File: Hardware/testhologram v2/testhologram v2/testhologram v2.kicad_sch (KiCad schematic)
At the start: 609 parts, among them U1 SM16106SC, U10 SM16106SC, U11 SM16106SC, U12 SM16106SC, U13 SM16106SC, U14 SM16106SC, U15 SM16106SC, U16 SM16106SC, U17 SM16106SC, U18 SM16106SC, U19 SM16106SC, U2 SM16106SC, U20 SM16106SC, U21 SM16106SC, U22 SM16106SC, U23 SM16106SC, U24 SM16106SC, U25 SM16106SC, U26 SM16106SC, U27 SM16106SC, U28 SM16106SC, U29 SM16106SC, U3 SM16106SC, U30 SM16106SC, U31 SM16106SC, U32 SM16106SC, U33 ESP32-S3-WROOM-1(N16R8), U4 SM16106SC, U5 SM16106SC, U6 SM16106SC, U7 SM16106SC, U8 SM16106SC, U9 SM16106SC

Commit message: added esp32 devboard docs into dataheets folder, updated hologram kicad schematic
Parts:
- added C33: 22uF/25v, symbol Device:C_Small
- added C34, C37, C38: 0.1uF/50v, symbol Device:C_Small
- added C35: 1uF/16v, symbol Device:C_Small
- added C36: 10uF/25v, symbol Device:C_Small
- added D1: 1N5819HW-7-F, symbol Device:D
- added D2, D3, D4: LESD5Z5.0CT1G, symbol Device:D_TVS
- added J1: USB_C_Receptacle_USB2.0_16P, symbol Connector:USB_C_Receptacle_USB2.0_16P
- added R33: 1M, symbol Device:R_Small_US
- added R34: 10k, symbol Device:R_Small_US
- added R35, R36: 5.11k, symbol Device:R_Small_US
- added SW1: SW_Reset, symbol Switch:SW_Push
- added SW2: SW_Boot, symbol Switch:SW_Push
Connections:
- net GND: now also U33.1 (GND), U33.40 (GND), U33.41 (GND), C33.2, C34.2, C35.2, C36.2, C37.2, C38.2, D2.1 (A1), D3.1 (A1), D4.1 (A1), J1.A1 (GND), J1.A12 (GND), J1.B1 (GND), J1.B12 (GND), R33.2, R35.2, R36.2, SW1.1, SW2.1
- net USB_D-: now reaches U33.13 (IO19)
- net USB_D-: now also D3.2 (A2), J1.A7 (D-), J1.B7 (D-)
- net USB_D+: now reaches U33.14 (IO20)
- net USB_D+: now also D4.2 (A2), J1.A6 (D+), J1.B6 (D+)
- net +3.3V: now reaches U33.2 (3V3)
- net +3.3V: now also C33.1, C34.1, R34.1
- net at U33.27 (IO0): now also C37.1, SW2.2
- net at U33.3 (EN): now also C35.1, C38.1, R34.2, SW1.2
- new net: J1.A5 (CC1), R35.1
- new net: D1.2 (A), D2.2 (A2), J1.A4 (VBUS), J1.A9 (VBUS), J1.B4 (VBUS), J1.B9 (VBUS)
- new net: J1.B5 (CC2), R36.1
- new net: J1.S1 (SHIELD), R33.1
- new net +5V: C36.1, D1.1 (K)
- no-connect marks 1 -> 8
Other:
- company: (none) -> Kaden Sparrow
- title: (none) -> Hologram spinnig panel

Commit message: worked on kicad
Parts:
- removed C37: 0.1uF/50v, symbol Device:C_Small
- added C39: 0.1uF/50v, symbol Device:C_Small
- added D5, D6, D7, D8: LESD5Z5.0CT1G, symbol Device:D_TVS
- added J2: Conn_01x06_Socket, symbol Connector:Conn_01x06_Socket
- added R37, R38, R39: 2.2k, symbol Device:R_Small_US
- added R40: 100k, symbol Device:R_Small_US
- added R41, R42, R43, R44, R45, R46: 33, symbol Device:R_Small_US
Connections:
- net +3.3V: now also R37.2, R38.2, R39.2
- net GND: now also C39.2, D5.1 (A1), D6.1 (A1), D7.1 (A1), D8.1 (A1), J2.2 (Pin_2), R40.1
- net USB_D+: now also R46.2; no longer U33.14 (IO20)
- net USB_D-: now also R45.2; no longer U33.13 (IO19)
- net VCC: now also J2.3 (Pin_3)
- net at U33.27 (IO0): now also R41.2; no longer SW2.2
- net SW_Reset: now reaches C35.1, C38.1, R34.2, SW1.2, U33.3 (EN)
- net at U33.4 (IO4): now also R42.1
- net at U33.5 (IO5): now also R43.1
- net at U33.6 (IO6): now also R44.1
- new net: R45.1, U33.13 (IO19)
- new net: R46.1, U33.14 (IO20)
- new net: D8.2 (A2), J2.1 (Pin_1), R40.2
- new net ENC_A: D5.2 (A2), J2.6 (Pin_6), R39.1, R42.2
- new net ENC_B: D6.2 (A2), J2.5 (Pin_5), R38.1, R43.2
- new net ENC_Z: D7.2 (A2), J2.4 (Pin_4), R37.1, R44.2
- new net SW_Boot: C39.1, R41.1, SW2.2
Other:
- note added: "1 PWM 2 GND 3 V+ 4 Z 5 B 6 A"
- moved on the sheet: C34, C35, C38, SW1

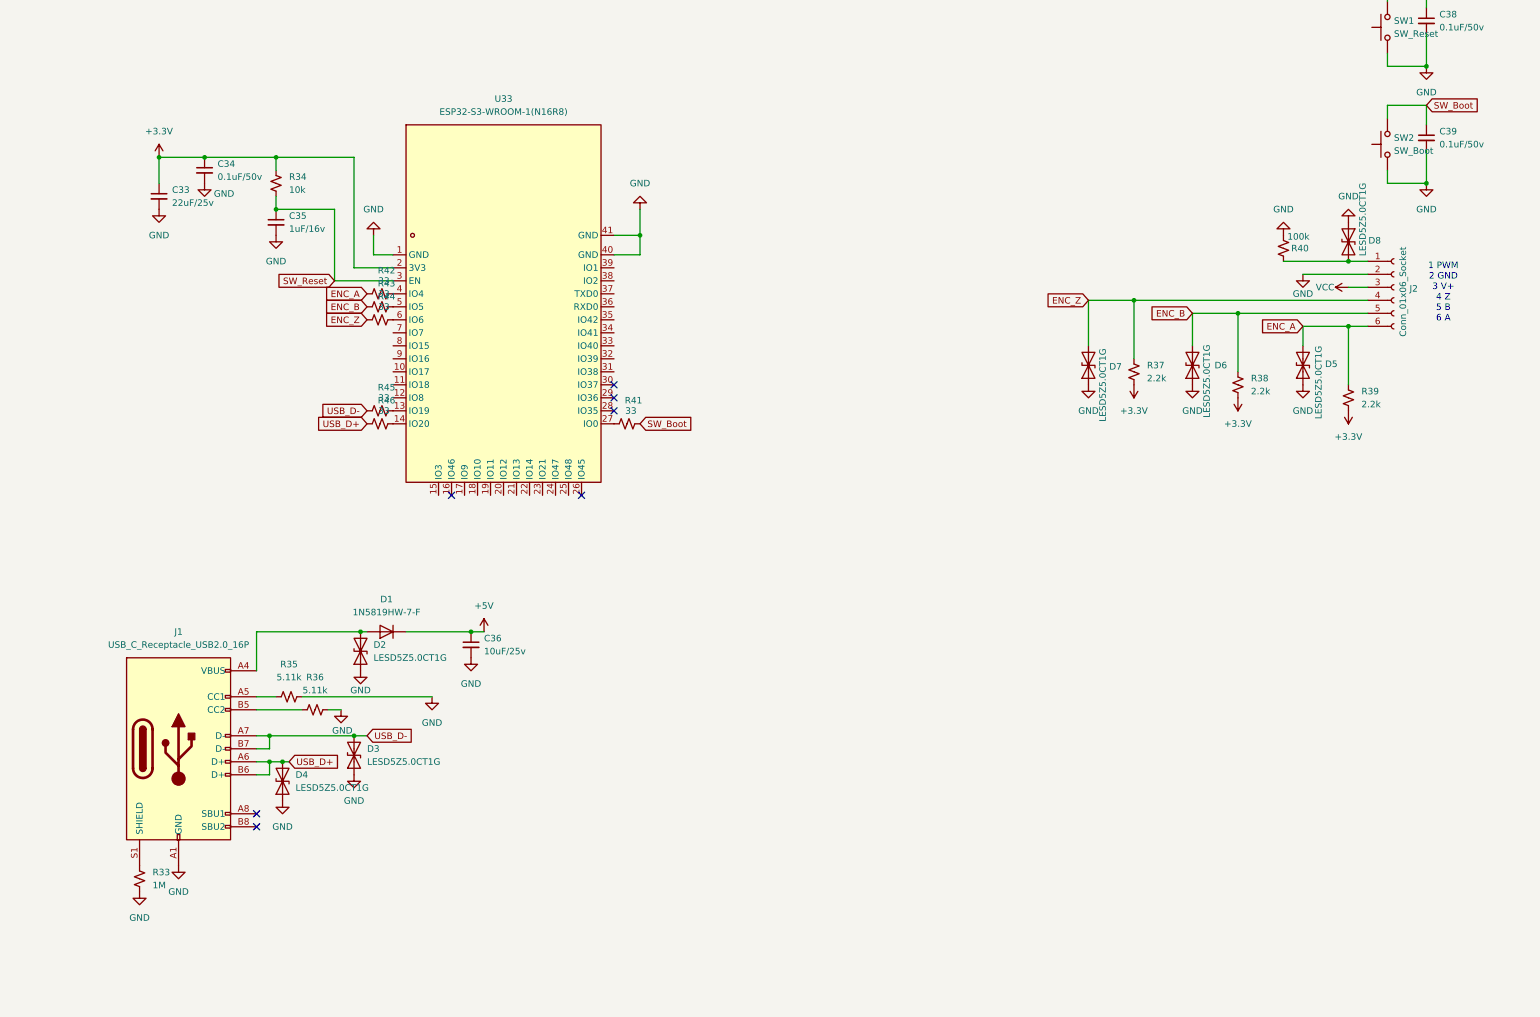
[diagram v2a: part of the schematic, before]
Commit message: added parts to schematic. added footprints/models
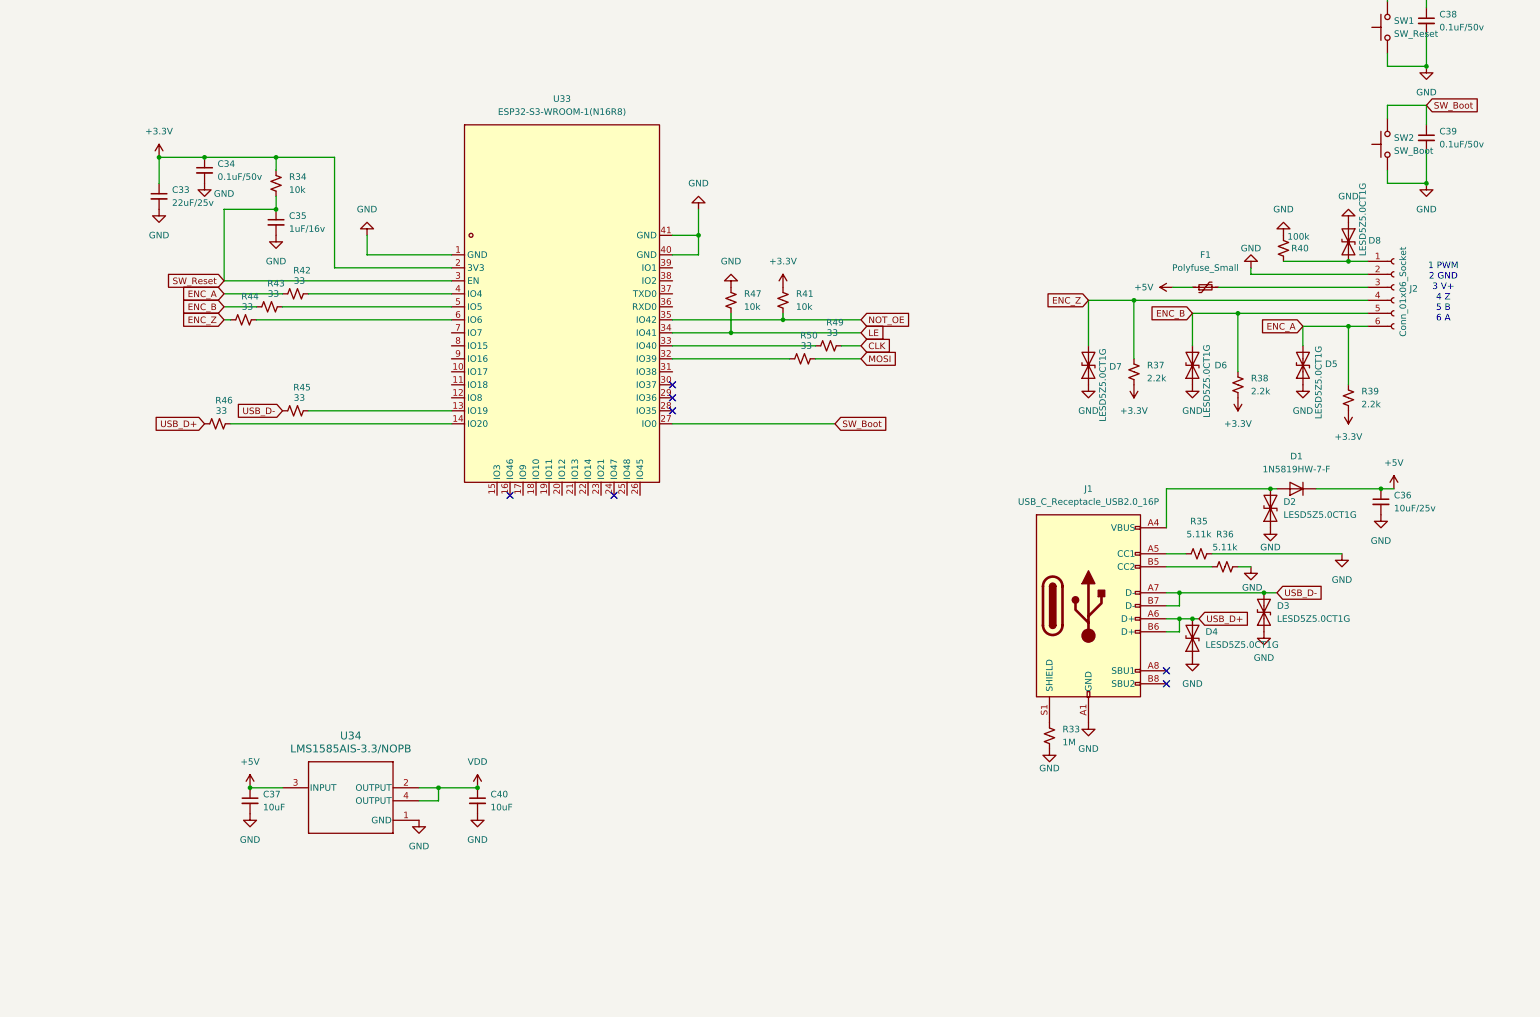
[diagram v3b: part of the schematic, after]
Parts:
- added C37, C40: 10uF, symbol Device:C_Small
- added F1: Polyfuse_Small, symbol Device:Polyfuse_Small
- added R47: 10k, symbol Device:R_Small_US
- added R49, R50: 33, symbol Device:R_Small_US
- added U34: LMS1585AIS-3.3/NOPB, KTT0003B, symbol LMS1585AIS-3.3/NOPB:LMS1585AIS-3.3_NOPB
- R41: value 33 -> 10k
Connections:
- net +3.3V: now also R41.1
- net +5V: now also C37.1, F1.1, U34.3 (INPUT)
- net CLK: now also R49.1
- net GND: now also C37.2, C40.2, R47.1, U34.1 (GND)
- net LE: now also U33.34 (IO41), R47.2
- net NOT_OE: now also R41.2, U33.35 (IO42)
- net SW_Boot: now also U33.27 (IO0); no longer R41.1
- net VCC: no longer J2.3 (Pin_3)
- net VDD: now also C40.1, U34.2 (OUTPUT), U34.4 (OUTPUT)
- net at U33.32 (IO39): now also R50.2
- net at U33.33 (IO40): now also R49.2
- new net: F1.2, J2.3 (Pin_3)
- new net MOSI: R50.1
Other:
- moved on the sheet: C36, D1, D2, D3, D4, J1, R33, R35, R36, R42, R43, R44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

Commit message: i did some kicad stuff
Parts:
- added U35: TPS7A5601RTER, easyeda:QFN-16_L3.0-W3.0-P0.50-TL-EP1.5-1, symbol easyeda:TPS7A5601RTER
- LED1, LED10, LED100, LED101, LED102, LED103, LED104, LED105, LED106, LED107, LED108, LED109, LED11, LED110, LED111, LED112, LED113, LED114, LED115, LED116, LED117, LED118, LED119, LED12, LED120, LED121, LED122, LED123, LED124, LED125, LED126, LED127, LED128, LED129, LED13, LED130, LED131, LED132, LED133, LED134, LED135, LED136, LED137, LED138, LED139, LED14, LED140, LED141, LED142, LED143, LED144, LED145, LED146, LED147, LED148, LED149, LED15, LED150, LED151, LED152, LED153, LED154, LED155, LED156, LED157, LED158, LED159, LED16, LED160, LED161, LED162, LED163, LED164, LED165, LED166, LED167, LED168, LED169, LED17, LED170, LED171, LED172, LED173, LED174, LED175, LED176, LED177, LED178, LED179, LED18, LED180, LED181, LED182, LED183, LED184, LED185, LED186, LED187, LED188, LED189, LED19, LED190, LED191, LED192, LED193, LED194, LED195, LED196, LED197, LED198, LED199, LED2, LED20, LED200, LED201, LED202, LED203, LED204, LED205, LED206, LED207, LED208, LED209, LED21, LED210, LED211, LED212, LED213, LED214, LED215, LED216, LED217, LED218, LED219, LED22, LED220, LED221, LED222, LED223, LED224, LED225, LED226, LED227, LED228, LED229, LED23, LED230, LED231, LED232, LED233, LED234, LED235, LED236, LED237, LED238, LED239, LED24, LED240, LED241, LED242, LED243, LED244, LED245, LED246, LED247, LED248, LED249, LED25, LED250, LED251, LED252, LED253, LED254, LED255, LED256, LED257, LED258, LED259, LED26, LED260, LED261, LED262, LED263, LED264, LED265, LED266, LED267, LED268, LED269, LED27, LED270, LED271, LED272, LED273, LED274, LED275, LED276, LED277, LED278, LED279, LED28, LED280, LED281, LED282, LED283, LED284, LED285, LED286, LED287, LED288, LED289, LED29, LED290, LED291, LED292, LED293, LED294, LED295, LED296, LED297, LED298, LED299, LED3, LED30, LED300, LED301, LED302, LED303, LED304, LED305, LED306, LED307, LED308, LED309, LED31, LED310, LED311, LED312, LED313, LED314, LED315, LED316, LED317, LED318, LED319, LED32, LED320, LED321, LED322, LED323, LED324, LED325, LED326, LED327, LED328, LED329, LED33, LED330, LED331, LED332, LED333, LED334, LED335, LED336, LED337, LED338, LED339, LED34, LED340, LED341, LED342, LED343, LED344, LED345, LED346, LED347, LED348, LED349, LED35, LED350, LED351, LED352, LED353, LED354, LED355, LED356, LED357, LED358, LED359, LED36, LED360, LED361, LED362, LED363, LED364, LED365, LED366, LED367, LED368, LED369, LED37, LED370, LED371, LED372, LED373, LED374, LED375, LED376, LED377, LED378, LED379, LED38, LED380, LED381, LED382, LED383, LED384, LED385, LED386, LED387, LED388, LED389, LED39, LED390, LED391, LED392, LED393, LED394, LED395, LED396, LED397, LED398, LED399, LED4, LED40, LED400, LED401, LED402, LED403, LED404, LED405, LED406, LED407, LED408, LED409, LED41, LED410, LED411, LED412, LED413, LED414, LED415, LED416, LED417, LED418, LED419, LED42, LED420, LED421, LED422, LED423, LED424, LED425, LED426, LED427, LED428, LED429, LED43, LED430, LED431, LED432, LED433, LED434, LED435, LED436, LED437, LED438, LED439, LED44, LED440, LED441, LED442, LED443, LED444, LED445, LED446, LED447, LED448, LED449, LED45, LED450, LED451, LED452, LED453, LED454, LED455, LED456, LED457, LED458, LED459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: footprint led-kt0805g:LED0805-R-RD -> easyeda:LED0805-RD
- U33: footprint easyeda2kicad:WIRELM-SMD_ESP32-S3-WROOM-1 -> esp32-s3-wroom-1:WIRELM-SMD_ESP32-S3-WROOM-1
- U34: footprint KTT0003B -> LMS1585AIS-3.3/NOPB:KTT0003B

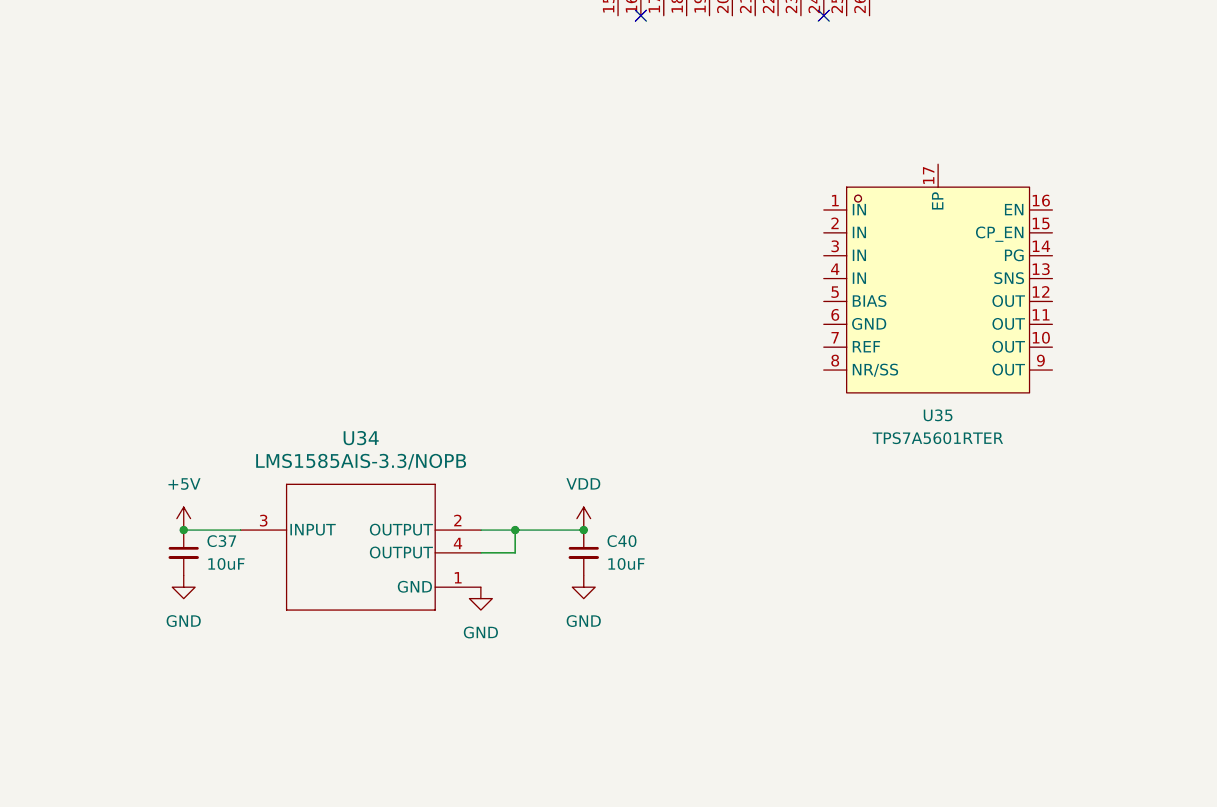
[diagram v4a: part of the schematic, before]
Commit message: added new buck converter
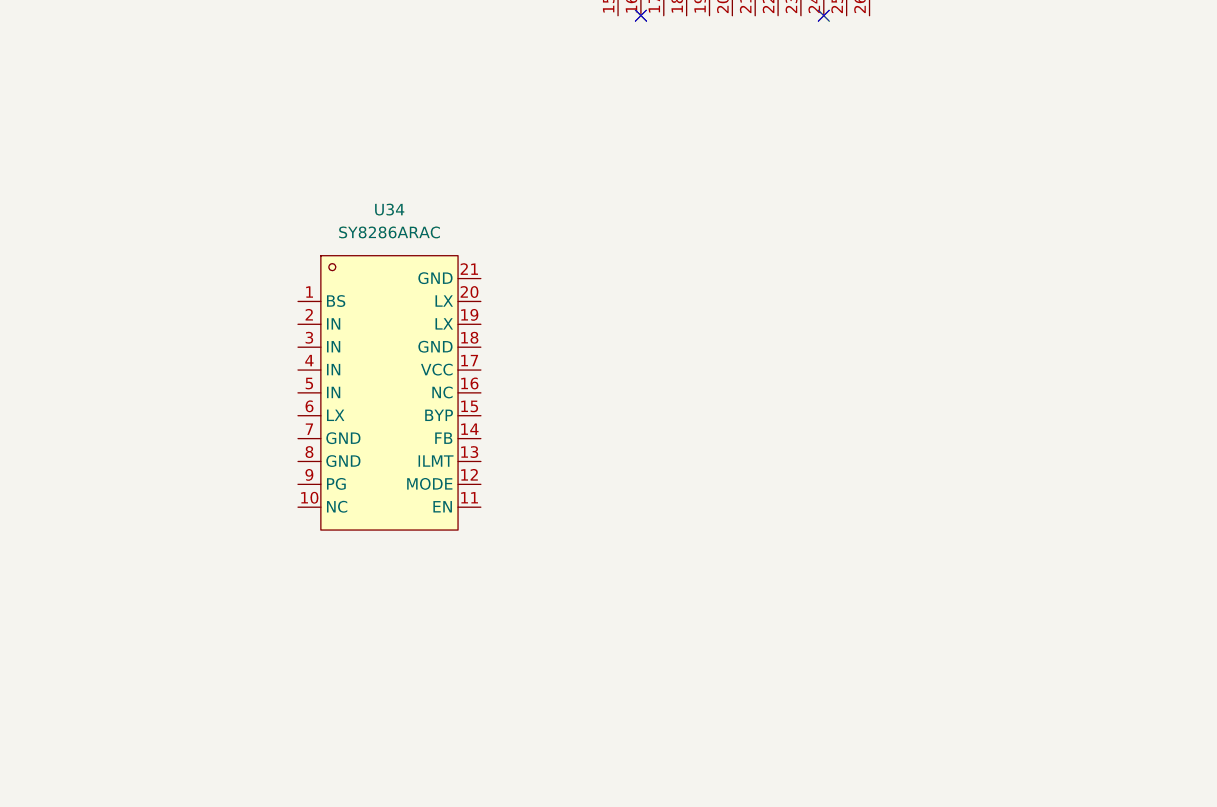
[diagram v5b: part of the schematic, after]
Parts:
- removed C37, C40: 10uF, symbol Device:C_Small
- removed U34: LMS1585AIS-3.3/NOPB, LMS1585AIS-3.3/NOPB:KTT0003B, symbol LMS1585AIS-3.3/NOPB:LMS1585AIS-3.3_NOPB
- removed U35: TPS7A5601RTER, easyeda:QFN-16_L3.0-W3.0-P0.50-TL-EP1.5-1, symbol easyeda:TPS7A5601RTER
- added U34: SY8286ARAC, easyeda:QFN-20_L3.0-W3.0-P0.45-BL-EP1.0, symbol easyeda:SY8286ARAC
